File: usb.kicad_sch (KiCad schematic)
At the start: 26 parts, among them J1 USB_C, U3 PI3USB102G, U9 USB3343-CP

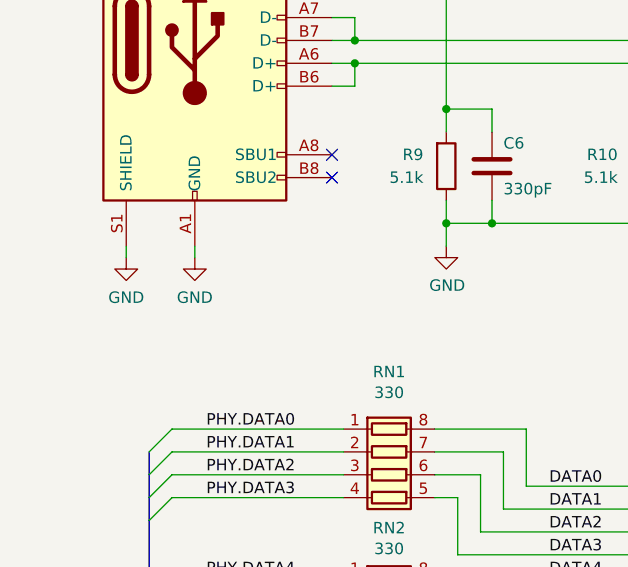
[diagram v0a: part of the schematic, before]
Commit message: add regulator for analog 3.3 V supply
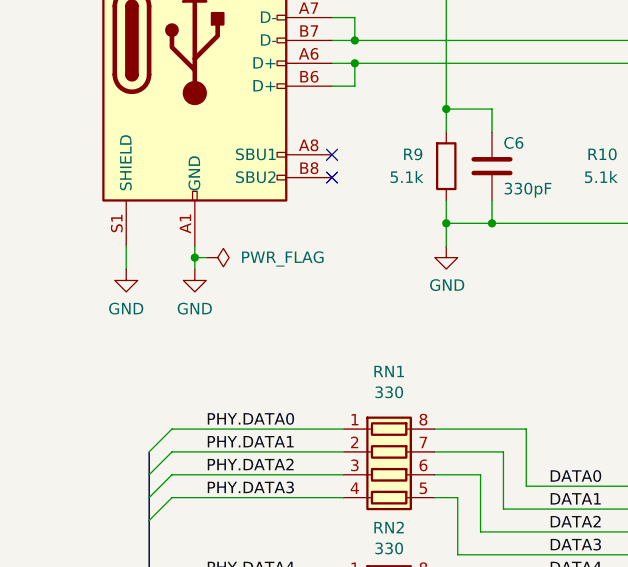
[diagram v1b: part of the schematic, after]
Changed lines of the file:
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@@
   (junction (at 146.05 111.76) (diameter 0) (color 0 0 0 0)
+  )
+  (junction (at 60.96 86.36) (diameter 0) (color 0 0 0 0)
   )
   (junction (at 148.59 152.4) (diameter 0) (color 0 0 0 0)
@@
     (stroke (width 0) (type default))
   )
-  (wire (pts (xy 53.34 85.09) (xy 53.34 86.36))
+  (wire (pts (xy 53.34 85.09) (xy 53.34 87.63))
     (stroke (width 0) (type default))
   )
@@
     (stroke (width 0) (type default))
   )
+  (wire (pts (xy 60.96 86.36) (xy 60.96 87.63))
+    (stroke (width 0) (type default))
+  )
   (wire (pts (xy 77.47 105.41) (xy 58.42 105.41))
     (stroke (width 0) (type default))
@@
   )
   (wire (pts (xy 143.51 143.51) (xy 146.05 143.51))
+    (stroke (width 0) (type default))
+  )
+  (wire (pts (xy 60.96 86.36) (xy 62.23 86.36))
     (stroke (width 0) (type default))
   )
@@
     )
   )
-  (symbol (lib_id "power:GND") (at 53.34 86.36 0) (unit 1)
+  (symbol (lib_id "power:GND") (at 53.34 87.63 0) (unit 1)
     (in_bom yes) (on_board yes) (dnp no) (fields_autoplaced)
-    (property "Reference" "#PWR040" (at 53.34 92.71 0)
-      (effects (font (size 1.27 1.27)) hide)
-    )
-    (property "Value" "GND" (at 53.34 90.8034 0)
-      (effects (font (size 1.27 1.27)))
-    )
-    (property "Footprint" "" (at 53.34 86.36 0)
-      (effects (font (size 1.27 1.27)) hide)
-    )
-    (property "Datasheet" "" (at 53.34 86.36 0)
+    (property "Reference" "#PWR040" (at 53.34 93.98 0)
+      (effects (font (size 1.27 1.27)) hide)
+    )
+    (property "Value" "GND" (at 53.34 92.0734 0)
+      (effects (font (size 1.27 1.27)))
+    )
+    (property "Footprint" "" (at 53.34 87.63 0)
+      (effects (font (size 1.27 1.27)) hide)
+    )
+    (property "Datasheet" "" (at 53.34 87.63 0)
       (effects (font (size 1.27 1.27)) hide)
     )
@@
     )
   )
+  (symbol (lib_id "power:PWR_FLAG") (at 62.23 86.36 270) (unit 1)
+    (in_bom yes) (on_board yes) (dnp no) (fields_autoplaced)
+    (property "Reference" "#FLG03" (at 64.135 86.36 0)
+      (effects (font (size 1.27 1.27)) hide)
+    )
+    (property "Value" "PWR_FLAG" (at 66.04 86.36 90)
+      (effects (font (size 1.27 1.27)) (justify left))
+    )
+    (property "Footprint" "" (at 62.23 86.36 0)
+      (effects (font (size 1.27 1.27)) hide)
+    )
+    (property "Datasheet" "~" (at 62.23 86.36 0)
+      (effects (font (size 1.27 1.27)) hide)
+    )
+    (pin "1")
+    (instances
+      (project "mainboard"
+        (path "/fb621148-8145-4217-9712-738e1b5a4823/00000000-0000-0000-0000-00005da7baf4"
+          (reference "#FLG03") (unit 1)
+        )
+        (path "/fb621148-8145-4217-9712-738e1b5a4823/00000000-0000-0000-0000-00005dcd9772"
+          (reference "#FLG03") (unit 1)
+        )
+      )
+    )
+  )
   (symbol (lib_id "power:+3V3") (at 217.17 64.77 270) (unit 1)
     (in_bom yes) (on_board yes) (dnp no)
@@
     )
   )
-  (symbol (lib_id "power:GND") (at 60.96 86.36 0) (unit 1)
+  (symbol (lib_id "power:GND") (at 60.96 87.63 0) (unit 1)
     (in_bom yes) (on_board yes) (dnp no) (fields_autoplaced)
-    (property "Reference" "#PWR041" (at 60.96 92.71 0)
-      (effects (font (size 1.27 1.27)) hide)
-    )
-    (property "Value" "GND" (at 60.96 90.8034 0)
-      (effects (font (size 1.27 1.27)))
-    )
-    (property "Footprint" "" (at 60.96 86.36 0)
-      (effects (font (size 1.27 1.27)) hide)
-    )
-    (property "Datasheet" "" (at 60.96 86.36 0)
-      (effects (font (size 1.27 1.27)) hide)
-    )
+    (property "Reference" "#PWR041" (at 60.96 93.98 0)
+      (effects (font (size 1.27 1.27)) hide)
+    )
+    (property "Value" "GND" (at 60.96 92.0734 0)
+      (effects (font (size 1.27 1.27)))
+    )
+    (property "Footprint" "" (at 60.96 87.63 0)
+      (effects (font (size 1.27 1.27)) hide)
+    )
+    (property "Datasheet" "" (at 60.96 87.63 0)
+      (effects (font (size 1.27 1.27)) hide)
+    )

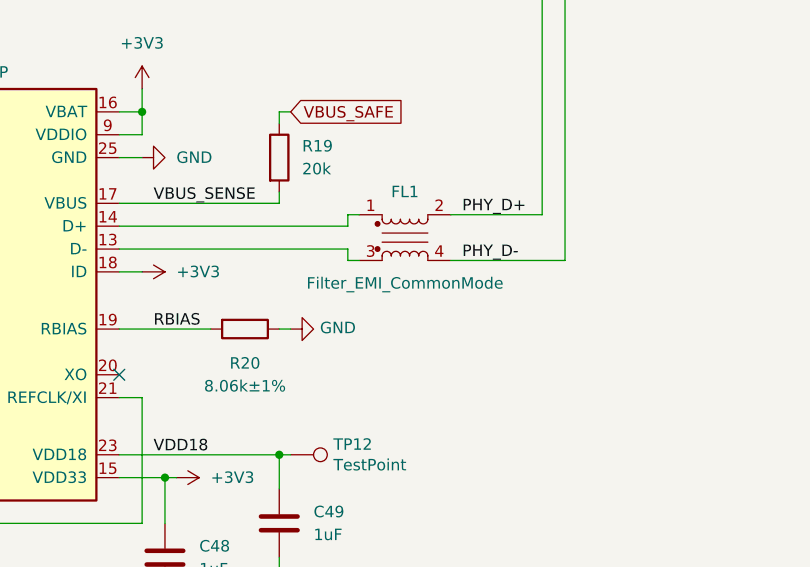
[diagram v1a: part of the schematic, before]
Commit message: add analog baseband common-mode chokes
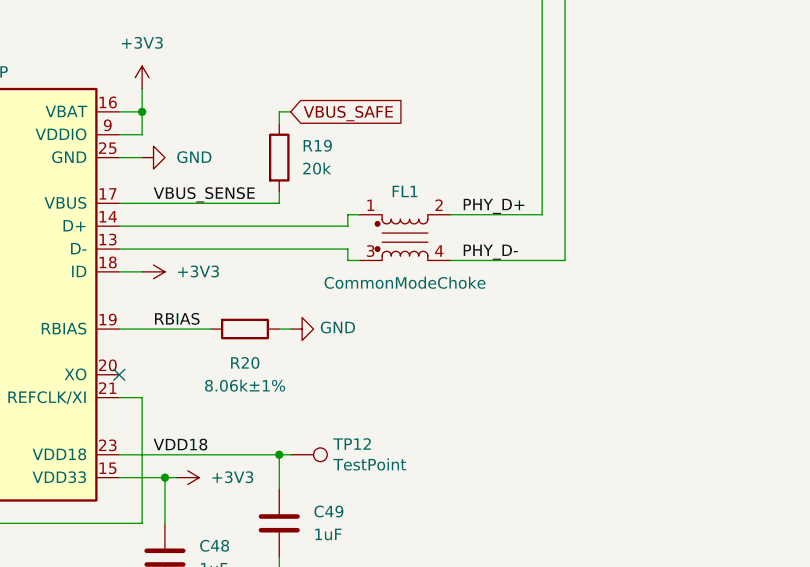
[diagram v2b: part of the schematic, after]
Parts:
- FL1: value Filter_EMI_CommonMode -> CommonModeChoke
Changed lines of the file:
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@@
       (effects (font (size 1.27 1.27)))
     )
-    (property "Value" "Filter_EMI_CommonMode" (at 175.26 130.81 0)
+    (property "Value" "CommonModeChoke" (at 175.26 130.81 0)
       (effects (font (size 1.27 1.27)))
     )

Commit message: layout wip
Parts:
- C5: footprint Capacitor_SMD:C_0402_1005Metric -> Capacitor_SMD:C_0201_0603Metric; Manufacturer Samsung -> Murata; Part Number CL05B102KB5NNNC -> GRM033R71E102KA01D; Substitution any equivalent -> GRM033R71E102KA01*
- C6, C7: footprint Capacitor_SMD:C_0402_1005Metric -> Capacitor_SMD:C_0201_0603Metric; Manufacturer Samsung -> Murata; Part Number CL05C331JB5NNNC -> GRM0335C1E331JA01D; Substitution any equivalent -> GRM0335C1E331JA01*
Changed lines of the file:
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@@
       (effects (font (size 1.27 1.27)) (justify left))
     )
-    (property "Footprint" "Capacitor_SMD:C_0402_1005Metric" (at 116.5352 80.01 0)
+    (property "Footprint" "Capacitor_SMD:C_0201_0603Metric" (at 116.5352 80.01 0)
       (effects (font (size 1.27 1.27)) hide)
     )
@@
       (effects (font (size 1.27 1.27)) hide)
     )
-    (property "Part Number" "CL05C331JB5NNNC" (at 115.57 76.2 0)
-      (effects (font (size 1.27 1.27)) hide)
-    )
-    (property "Substitution" "any equivalent" (at 115.57 76.2 0)
-      (effects (font (size 1.27 1.27)) hide)
-    )
-    (property "Description" "CAP CER 330PF 50V C0G/NP0 0402" (at 115.57 76.2 0)
-      (effects (font (size 1.27 1.27)) hide)
-    )
-    (property "Manufacturer" "Samsung" (at 115.57 76.2 0)
+    (property "Part Number" "GRM0335C1E331JA01D" (at 115.57 76.2 0)
+      (effects (font (size 1.27 1.27)) hide)
+    )
+    (property "Substitution" "GRM0335C1E331JA01*" (at 115.57 76.2 0)
+      (effects (font (size 1.27 1.27)) hide)
+    )
+    (property "Description" "CAP CER 330PF 25V C0G/NP0 0201" (at 115.57 76.2 0)
+      (effects (font (size 1.27 1.27)) hide)
+    )
+    (property "Manufacturer" "Murata" (at 115.57 76.2 0)
       (effects (font (size 1.27 1.27)) hide)
     )
@@
       (effects (font (size 1.27 1.27)) (justify left))
     )
-    (property "Footprint" "Capacitor_SMD:C_0402_1005Metric" (at 94.9452 80.01 0)
+    (property "Footprint" "Capacitor_SMD:C_0201_0603Metric" (at 94.9452 80.01 0)
       (effects (font (size 1.27 1.27)) hide)
     )
@@
       (effects (font (size 1.27 1.27)) hide)
     )
-    (property "Part Number" "CL05C331JB5NNNC" (at 93.98 76.2 0)
-      (effects (font (size 1.27 1.27)) hide)
-    )
-    (property "Substitution" "any equivalent" (at 93.98 76.2 0)
-      (effects (font (size 1.27 1.27)) hide)
-    )
-    (property "Description" "CAP CER 330PF 50V C0G/NP0 0402" (at 93.98 76.2 0)
-      (effects (font (size 1.27 1.27)) hide)
-    )
-    (property "Manufacturer" "Samsung" (at 93.98 76.2 0)
+    (property "Part Number" "GRM0335C1E331JA01D" (at 93.98 76.2 0)
+      (effects (font (size 1.27 1.27)) hide)
+    )
+    (property "Substitution" "GRM0335C1E331JA01*" (at 93.98 76.2 0)
+      (effects (font (size 1.27 1.27)) hide)
+    )
+    (property "Description" "CAP CER 330PF 25V C0G/NP0 0201" (at 93.98 76.2 0)
+      (effects (font (size 1.27 1.27)) hide)
+    )
+    (property "Manufacturer" "Murata" (at 93.98 76.2 0)
       (effects (font (size 1.27 1.27)) hide)
     )
@@
       (effects (font (size 1.27 1.27)) (justify left))
     )
-    (property "Footprint" "Capacitor_SMD:C_0402_1005Metric" (at 160.9852 85.09 0)
+    (property "Footprint" "Capacitor_SMD:C_0201_0603Metric" (at 160.9852 85.09 0)
       (effects (font (size 1.27 1.27)) hide)
     )
@@
       (effects (font (size 1.27 1.27)) hide)
     )
-    (property "Part Number" "CL05B102KB5NNNC" (at 160.02 81.28 0)
-      (effects (font (size 1.27 1.27)) hide)
-    )
-    (property "Substitution" "any equivalent" (at 160.02 81.28 0)
-      (effects (font (size 1.27 1.27)) hide)
-    )
-    (property "Description" "CAP CER 1000PF 50V X7R 0402" (at 160.02 81.28 0)
-      (effects (font (size 1.27 1.27)) hide)
-    )
-    (property "Manufacturer" "Samsung" (at 160.02 81.28 0)
-      (effects (font (size 1.27 1.27)) hide)
-    )
+    (property "Part Number" "GRM033R71E102KA01D" (at 160.02 81.28 0)
+      (effects (font (size 1.27 1.27)) hide)
+    )
+    (property "Substitution" "GRM033R71E102KA01*" (at 160.02 81.28 0)
+      (effects (font (size 1.27 1.27)) hide)
+    )
+    (property "Description" "CAP CER 1000PF 25V X7R 0201" (at 160.02 81.28 0)
+      (effects (font (size 1.27 1.27)) hide)
+    )
+    (property "Manufacturer" "Murata" (at 160.02 81.28 0)
+      (effects (font (size 1.27 1.27)) hide)
+    )

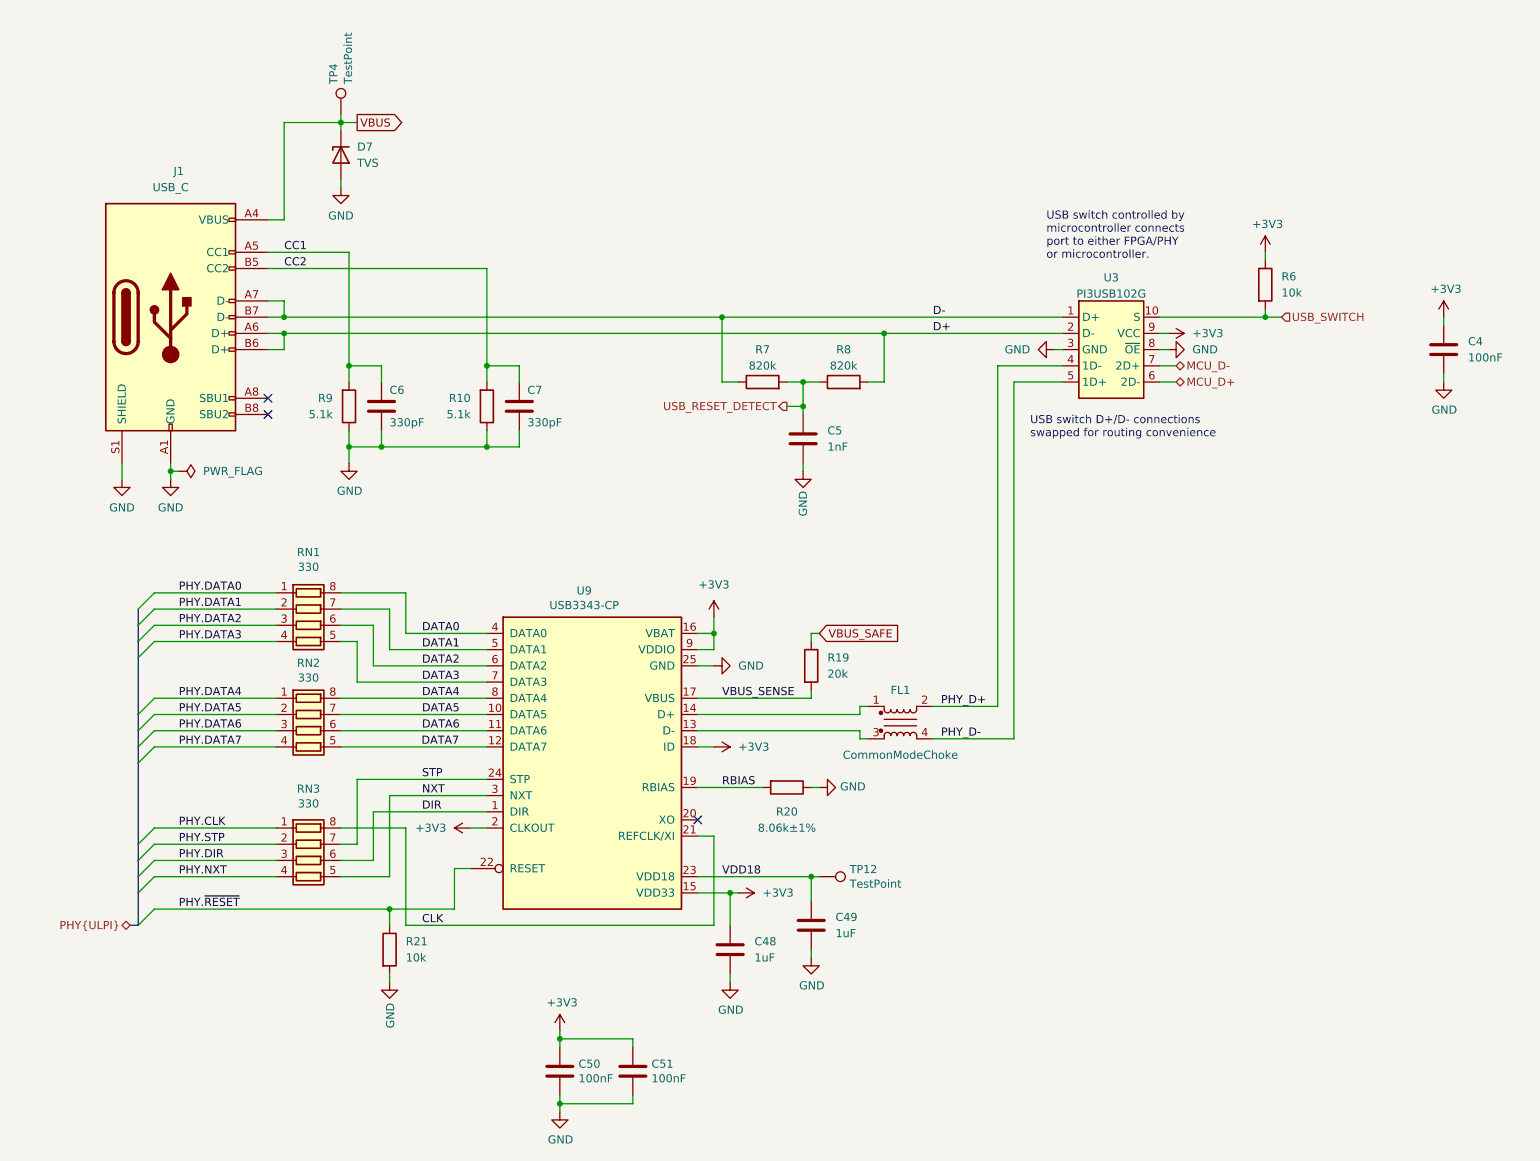
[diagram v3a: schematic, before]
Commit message: complete initial layout
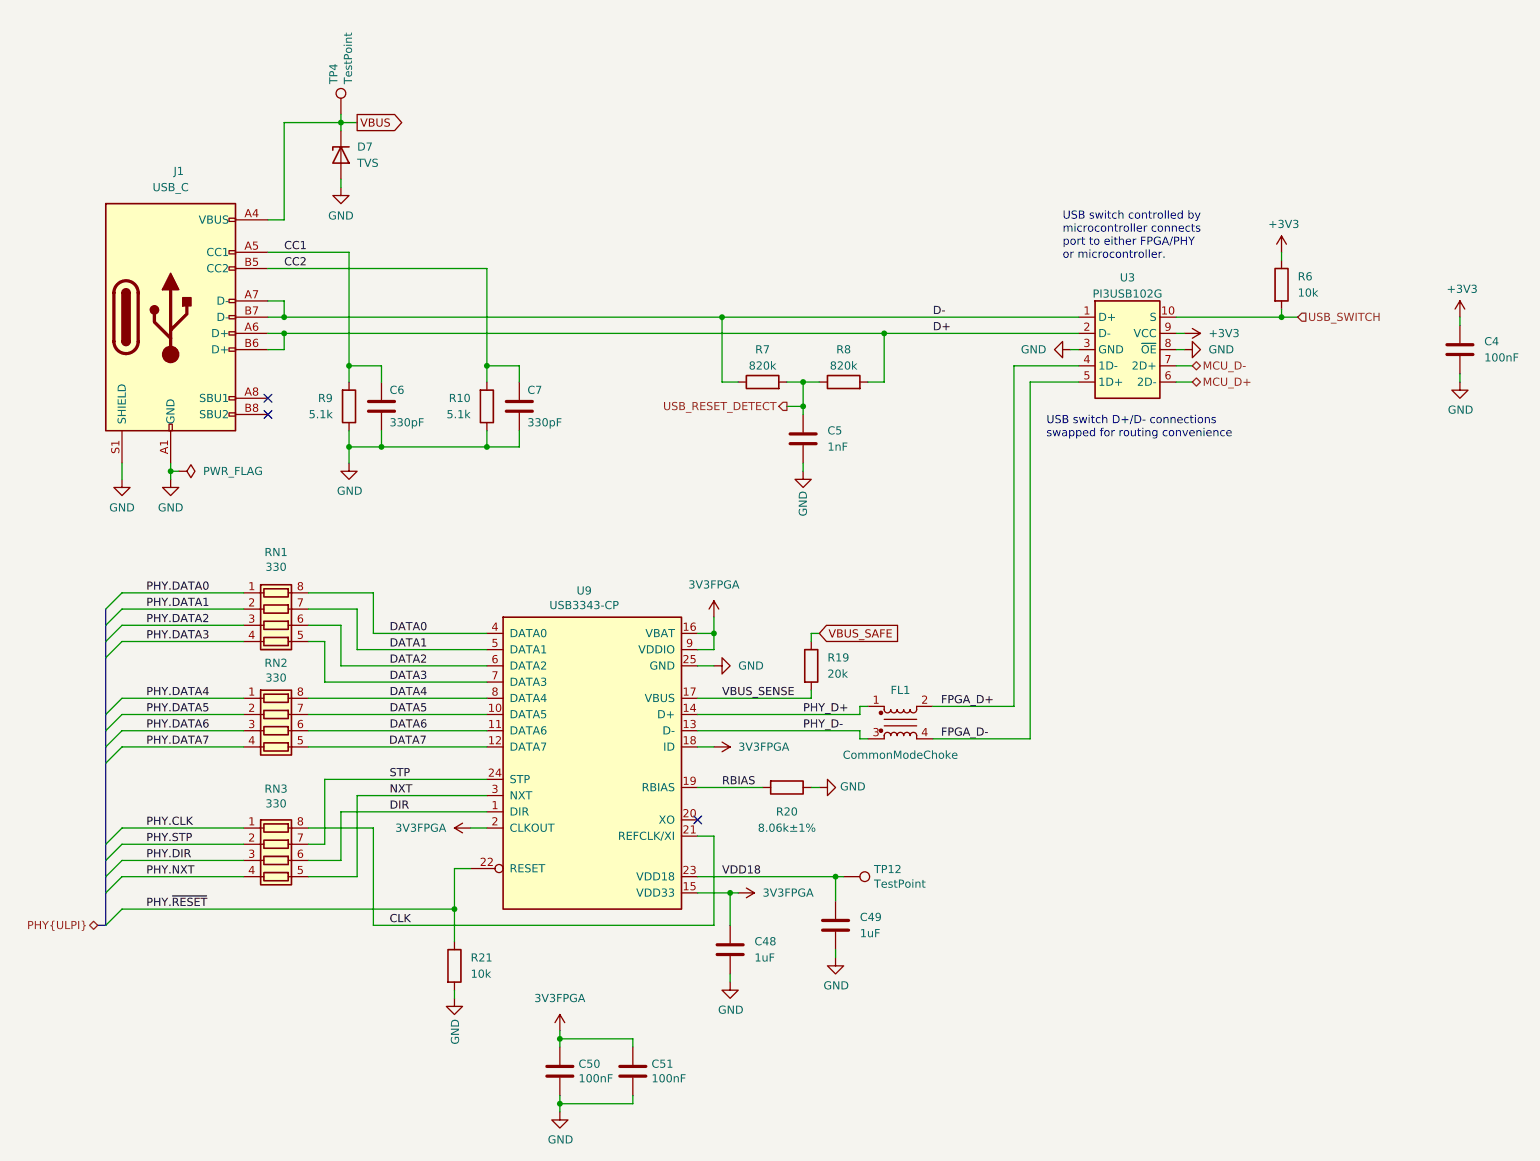
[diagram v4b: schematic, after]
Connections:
- net +3V3: no longer C48.1, C50.1, C51.1, U9.15 (VDD33), U9.16 (VBAT), U9.18 (ID), U9.2 (CLKOUT), U9.9 (VDDIO)
- net PHY_D+: now also FL1.1, U9.14 (D+); no longer FL1.2, U3.4 (1D-)
- net PHY_D-: now also FL1.3, U9.13 (D-); no longer FL1.4, U3.5 (1D+)
- new net 3V3FPGA: C48.1, C50.1, C51.1, U9.15 (VDD33), U9.16 (VBAT), U9.18 (ID), U9.2 (CLKOUT), U9.9 (VDDIO)
- new net FPGA_D+: FL1.2, U3.4 (1D-)
- new net FPGA_D-: FL1.4, U3.5 (1D+)
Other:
- moved on the sheet: C4, C49, R21, R6, RN1, RN2, RN3, TP12, U3
